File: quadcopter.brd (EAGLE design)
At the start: 185.1 x 185.1 mm, 69 parts, among them J1 AVR_SPI_PRG_6NS, Q1 2.6A, Q2 2.6A, Q3 2.6A, Q4 2.6A, U1 ATMEGA128RFA1, U2 IMU_LSM9DS1TR, Y1 16MHz

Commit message: Board ready for final review
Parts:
- removed D10: Green, LEDs:LED_OVS5MXBCR4
- removed D9: Blue, LEDs:LED_OVS5MXBCR4
- removed R11, R5: 100, quadparts_prebuilt:RESC2012X60_HS
- added Q5, Q6: 2.6A, quadparts_connie:N_MOSFET_SI2302CDS_T1_E3
- added SW1: PUSHBUTTON_SMD-VERTICAL, quadparts_prebuilt:TE_FSM8JSMA_HS
- D1, D2, D3, D4: value (none) -> 360mV
- R10, R9: value 100 -> 11
- moved R10 53.0 mm to (-13.6, -18.0), flipped to the bottom, turned to 270 degrees
- moved R9 31.7 mm to (13.2, -18.5), flipped to the bottom, turned to 270 degrees
- moved J1 13.8 mm to (-0.20, -16.3)
- moved D5 5.20 mm to (-20.4, -20.2)
- moved C13 5.10 mm to (-30.3, 15.9)
- moved D6 4.88 mm to (20.1, -20.8), flipped to the bottom
- moved C27 3.83 mm to (-5.80, 16.5), turned to 90 degrees
- moved C24 3.72 mm to (-23.6, 4.70), turned to 270 degrees
- moved C12 3.68 mm to (-9.60, 19.5), turned to 0 degrees
- moved D3 3.31 mm to (66.6, 0.40)
- moved D1 3.12 mm to (-64.0, -1.60)
- moved C9 2.66 mm to (-18.9, 3.20), turned to 270 degrees
- moved Y1 2.30 mm to (-9.61, 14.7)
- moved D4 2.19 mm to (-1.30, 69.4)
- moved C20 1.97 mm to (-3.40, 6.40)
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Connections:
- removed net N$11: J1.3
- removed net N$12: J1.5
- removed net N$18: D9.A, R9.2
- removed net N$19: D10.A, R5.1
- removed net N$20: R5.2, U1.14
- removed net N$26: R9.1, U1.15
- removed net N$28: D6.A, R11.1
- removed net N$6 (its old number): JP2.RXI
- removed net N$7: JP2.TXO
- removed net N$8: J1.1
- removed net N$9: J1.4
- new net PB6: Q5.1G, U1.42
- new net PB7: Q6.1G, U1.43
- net BAT_GND: now also Q5.2S, Q6.2S; no longer D5.C, D6.C
- net GND: now also SW1.3, SW1.4; no longer D10.C, D9.C
- net MISO: now also J1.1
- net MOSI: now also J1.4
- net N$2: now also D6.C, Q5.3D; no longer JP1.TXO
- net N$3: now also D6.A, R9.2; no longer JP1.RXI
- net N$4: now also D5.C, Q6.3D; no longer C1.2
- net RESET: now also C1.2, J1.5, SW1.1, SW1.2
- net RX0: now also JP1.TXO
- net RX1: now also JP2.TXO
- net SCK: now also J1.3
- net TX0: now also JP1.RXI
- net TX1: now also JP2.RXI
- net VBAT: now also R9.1; no longer R11.2
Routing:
- net N$6: track 90.3 -> 4.60 mm, vias 1 -> 0
- net 3V: track 139.0 -> 58.6 mm, vias 2 -> 9
- net N$19: track 80.3 -> 0.00 mm
- net PB6: track 0.00 -> 53.8 mm, vias 0 -> 1
- net N$26: track 50.6 -> 0.00 mm
- net N$28: track 50.2 -> 0.00 mm
- net N$18: track 44.7 -> 0.00 mm
- net TX0: track 0.00 -> 44.1 mm, vias 0 -> 2
- net SCK: track 0.00 -> 43.8 mm, vias 0 -> 2
- net TX1: track 0.00 -> 42.5 mm
- net RESET: track 40.2 -> 82.5 mm, vias 0 -> 2
- net MISO: track 0.00 -> 41.8 mm, vias 0 -> 1
- net RX1: track 0.00 -> 40.5 mm
- net RX0: track 0.00 -> 39.8 mm
- net MOSI: track 0.00 -> 38.4 mm, vias 0 -> 2
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
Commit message: Fixed new board errors
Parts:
- moved C22 15.0 mm to (-0.80, -4.10)
- moved C20 8.91 mm to (-3.90, -2.50), turned to 270 degrees
- moved Q6 8.38 mm to (-20.7, -4.00), turned to 180 degrees
- moved C23 7.43 mm to (-0.80, 4.10), turned to 180 degrees
- moved C9 5.30 mm to (-19.1, 8.50), turned to 0 degrees
- moved C24 4.57 mm to (-25.8, 8.70), turned to 0 degrees
- moved R12 3.92 mm to (-3.90, 7.20)
- moved R8 2.73 mm to (0.10, 7.20), turned to 180 degrees
- moved U1 2.64 mm to (-22.8, 16.3)
- moved Y1 2.64 mm to (-11.7, 16.3)
- moved C27 2.64 mm to (-7.90, 18.1)
- moved C12 2.64 mm to (-11.7, 21.1)
- moved C26 2.64 mm to (-7.90, 14.2)
- moved U$1 2.40 mm to (-22.6, 30.8)
- moved SW1 2.28 mm to (-20.8, -0.90), flipped to the top, turned to 90 degrees
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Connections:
- removed net N$36: R12.2, U2.SDA/SDI/SDO
- net SDA: now also R12.2, U2.SDA/SDI/SDO
- net VBAT: now also U$3.3
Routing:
- net VBAT: track 138.1 -> 309.0 mm, vias 7 -> 3
- net SCL: track 69.7 -> 110.9 mm, vias 2 -> 1
- net TX0: track 44.1 -> 82.0 mm, vias 2 -> 1
- net PB7: track 23.7 -> 57.4 mm
- net SDA: track 57.2 -> 74.7 mm
- net N$24: track 24.4 -> 40.4 mm
- net PB6: track 53.8 -> 65.9 mm, vias 1 -> 3
- net BAT_GND: track 140.3 -> 131.7 mm
- net 3V: track 58.6 -> 50.2 mm, vias 9 -> 11
- net RFANT: track 11.9 -> 4.86 mm
- net N$4: track 10.4 -> 15.8 mm, vias 0 -> 2
- net PB5: track 81.8 -> 86.0 mm
- net SCK: track 43.8 -> 39.8 mm, vias 2 -> 1
- net RX0: track 39.8 -> 43.3 mm, vias 0 -> 2
- net PE4: track 106.7 -> 103.6 mm, vias 1 -> 2
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- added copper zone on layer 1, net GND
- added copper zone on layer 15, net N$7
- added copper zone on layer 2, net N$7
- removed copper zone on layer 1, net N$35

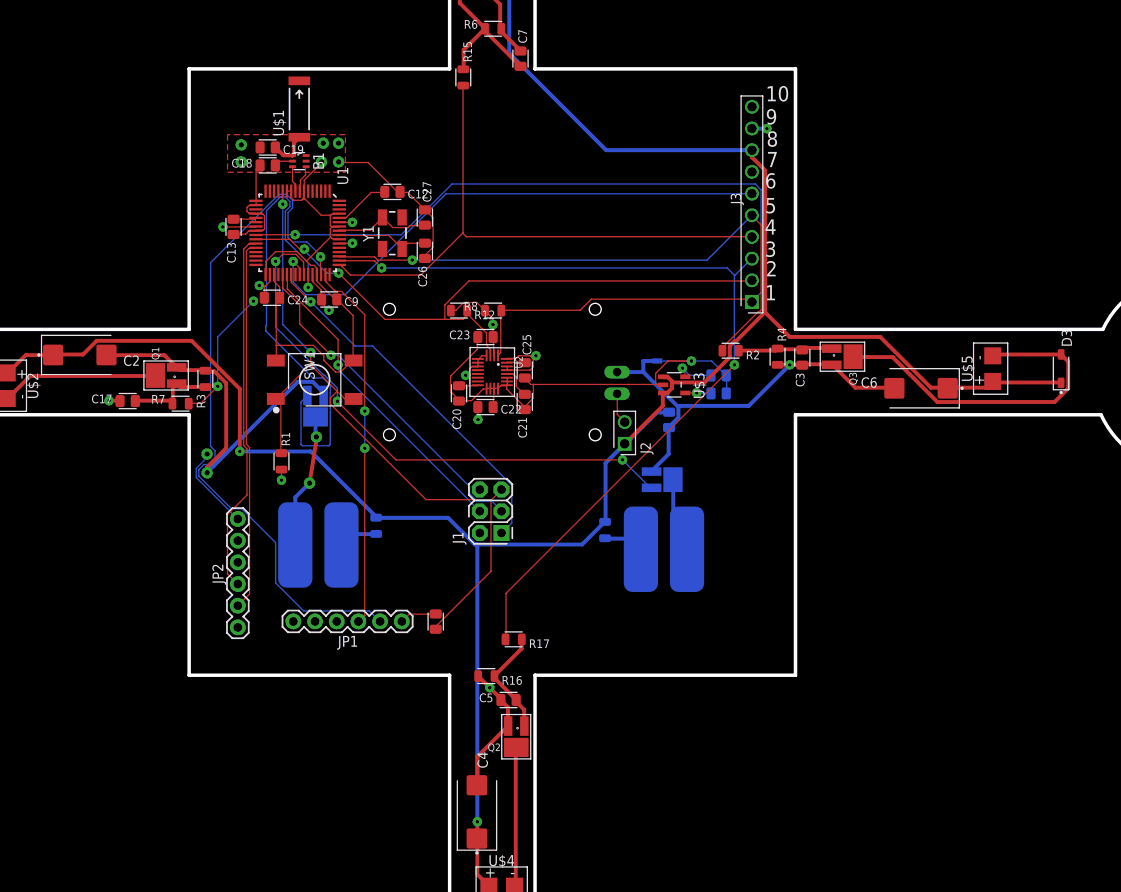
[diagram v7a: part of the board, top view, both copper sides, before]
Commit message: more board fixes
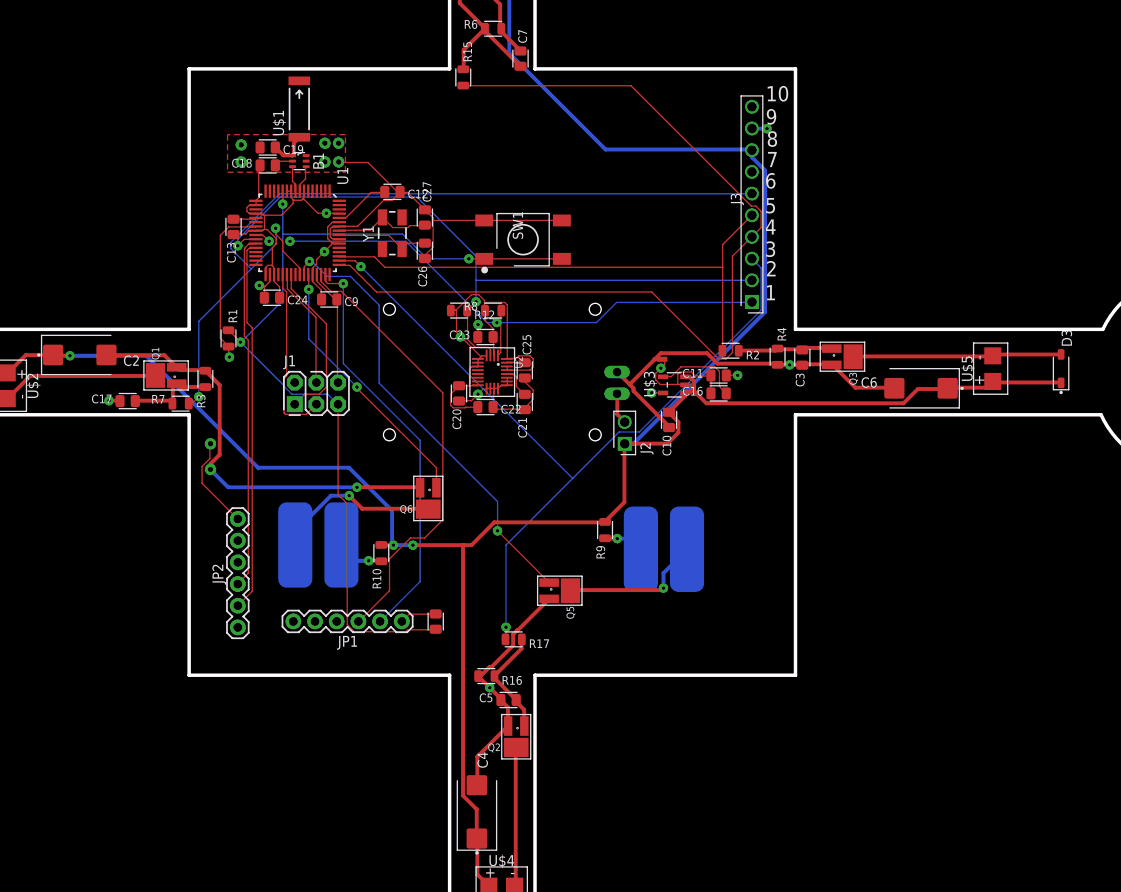
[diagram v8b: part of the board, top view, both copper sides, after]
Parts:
- moved SW1 29.4 mm to (3.60, 15.5)
- moved J1 24.6 mm to (-20.6, -2.50), turned to 0 degrees
- moved Q5 17.7 mm to (7.90, -25.6), flipped to the top, turned to 270 degrees
- moved Q6 17.1 mm to (-7.50, -14.8), flipped to the top
- moved R1 15.7 mm to (-30.9, 3.94)
- moved R10 3.26 mm to (-13.0, -21.2), flipped to the top
- moved NET_BRIDGE 0.63 mm to (19.9, 1.50), flipped to the top, turned to 180 degrees
- flipped C10 to the top
- flipped C11 to the top
- flipped C16 to the top
- flipped R9 to the top
- turned U$3 to 90 degrees
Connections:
- net RX0: now also U1.46; no longer U1.47
- net TX0: now also U1.47; no longer U1.46
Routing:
- net SCL: track 110.9 -> 69.2 mm, vias 1 -> 3
- net PE3: track 68.4 -> 109.8 mm
- net 3V: track 50.2 -> 87.6 mm, vias 11 -> 6
- net TX0: track 82.0 -> 48.2 mm
- net PB7: track 57.4 -> 31.2 mm, vias 1 -> 2
- net GND: track 169.3 -> 143.2 mm, vias 8 -> 11
- net MISO: track 42.7 -> 19.4 mm, vias 1 -> 0
- net MOSI: track 37.1 -> 14.1 mm, vias 1 -> 0
- net RESET: track 85.6 -> 107.2 mm, vias 2 -> 3
- net SCK: track 39.8 -> 20.9 mm, vias 1 -> 0
- net N$24: track 40.4 -> 24.4 mm
- net PB6: track 65.9 -> 52.8 mm, vias 3 -> 2
- net PB5: track 86.0 -> 99.1 mm, vias 3 -> 2
- net BAT_GND: track 131.7 -> 142.9 mm, vias 6 -> 7
- net VBAT: track 309.0 -> 319.6 mm, vias 3 -> 4
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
